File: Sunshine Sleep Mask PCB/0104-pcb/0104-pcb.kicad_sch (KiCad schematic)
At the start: 7 parts, among them J1 Conn_01x04, J2 Conn_01x02, J3 Conn_01x02, J4 Conn_02x15_Counter_Clockwise, U5 MAX98357A

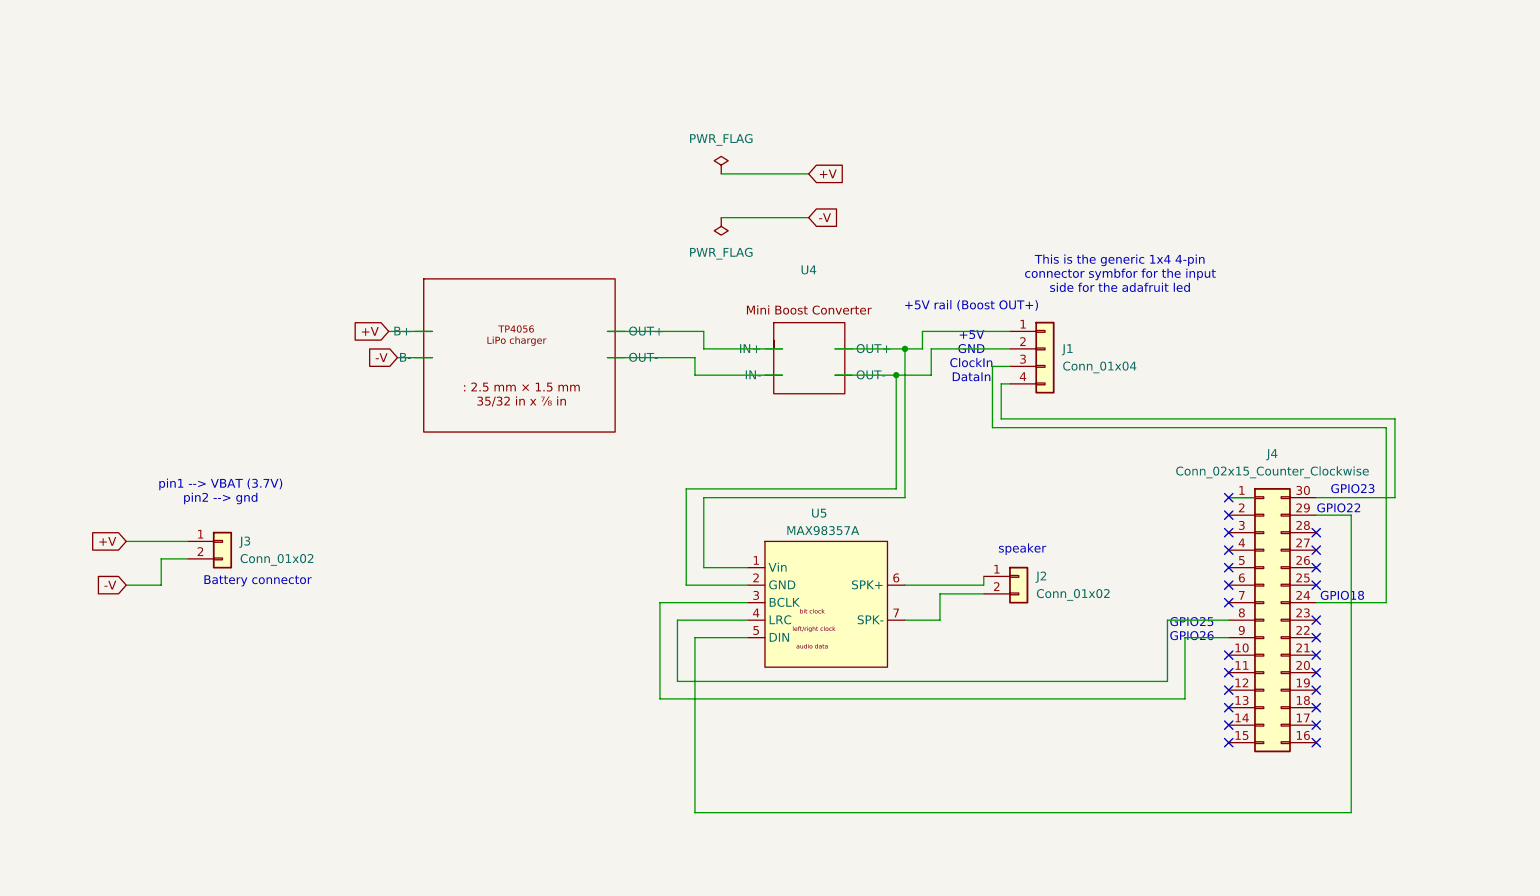
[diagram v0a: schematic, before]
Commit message: 0104- pcb + customized footprint
I created a new pcb editor + schematic where I copied the clay-0331. Then I made 3 customized footprints for the amplifier, charger LiPo, and for the boost converter. Similarly I was able to wire them in the pcb editor, yet there seems to be errors with the pcb constrains
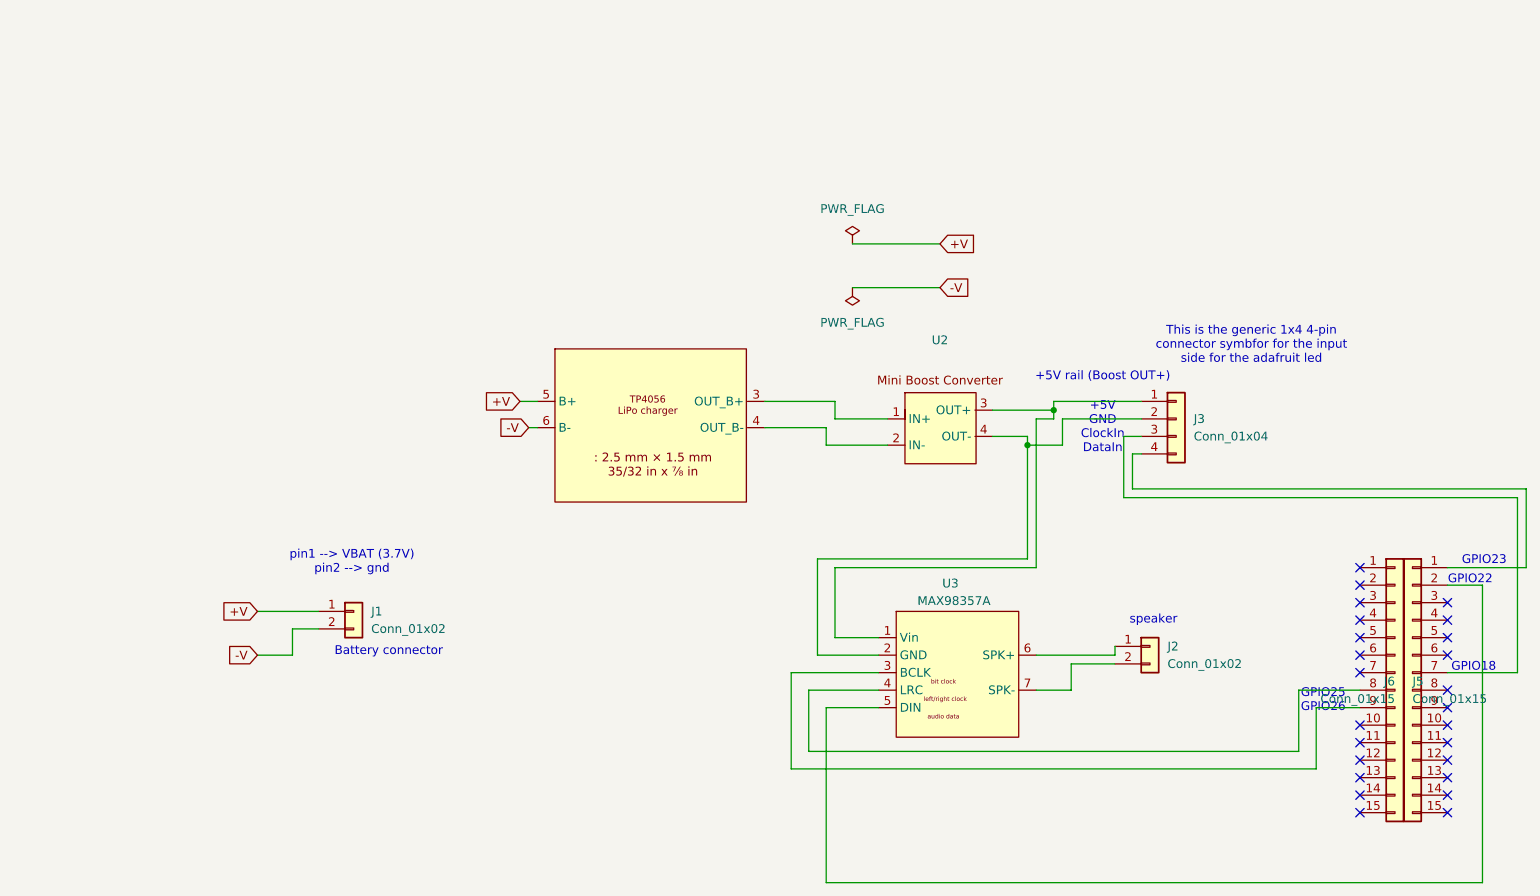
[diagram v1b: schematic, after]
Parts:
- removed J4: Conn_02x15_Counter_Clockwise, symbol Connector_Generic:Conn_02x15_Counter_Clockwise
- added J5, J6: Conn_01x15, Connector_PinSocket_2.54mm:PinSocket_1x15_P2.54mm_Vertical, symbol Connector_Generic:Conn_01x15
- U1: renamed from U3; footprint Connector_PinHeader_2.54mm:PinHeader_1x04_P2.54mm_Vertical -> Library_customized_0104:TP4056-18650
- U2: renamed from U4; footprint Connector_PinHeader_2.54mm:PinHeader_1x04_P2.54mm_Vertical -> Library_customized_0104:boost_converter
- U3: renamed from U5; footprint (none) -> Library_customized_0104:amplifier_github
- renumbered J3 to J1, J1 to J3
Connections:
- net +V: now also U1.5 (B+); no longer U1. (OUT-)
- net -V: now also U1.6 (B-); no longer U1. (OUT-)
- net at J3.1 (Pin_1), U3.1 (Vin): now also U2.3 (OUT+); no longer U2. (OUT-)
- net at J3.2 (Pin_2), U3.2 (GND): now also U2.4 (OUT-); no longer U2. (OUT-)
- net at U3.3 (BCLK): now also J5.9 (Pin_9)
- net at U3.4 (LRC): now also J5.8 (Pin_8)
- net at U3.5 (DIN): now also J6.2 (Pin_2)
- net at J3.3 (Pin_3): now also J6.7 (Pin_7)
- net at J3.4 (Pin_4): now also J6.1 (Pin_1)
- new net: U1.3 (OUT_B+), U2.1 (IN+)
- new net: U1.4 (OUT_B-), U2.2 (IN-)
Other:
- moved on the sheet: J1, J2, J3, U3

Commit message: Clay 0408 Changes
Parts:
- removed J2: Conn_01x02, Connector_PinHeader_2.54mm:PinHeader_1x02_P2.54mm_Vertical, symbol Connector_Generic:Conn_01x02
- removed J6: Conn_01x15, Connector_PinSocket_2.54mm:PinSocket_1x15_P2.54mm_Vertical, symbol Connector_Generic:Conn_01x15
- J5: value Conn_01x15 -> ESP32_WROOM; footprint Connector_PinSocket_2.54mm:PinSocket_1x15_P2.54mm_Vertical -> RF_Module:ESP32_WROOM_DevKit_30Pin_Custom
- U2: footprint Library_customized_0104:boost_converter -> Library_customized_0104:Boost_Converter_Clay_Custom
- U3: footprint Library_customized_0104:amplifier_github -> Library_customized_0104:adafruit-MAX98357
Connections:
- net at J3.1 (Pin_1), U2.3 (VOUT), U3.1 (Vin): now also J5.15 (VIN)
- net GND: now reaches J3.2 (Pin_2), U3.2 (GND)
- net GND: now also J5.14 (GND), J5.29 (GND), U1.4 (OUT-), U2.2 (GND); no longer U2.4 (OUT-)
- net at U3.3 (SV): no longer J5.9 (Pin_9)
- net at U3.4 (GAIN): no longer J5.8 (Pin_8)
- net at U3.5 (DIN): now also J5.26 (GPIO4)
- net at U3.6 (BCLK): now also J5.27 (GPIO2)
- net at U3.7 (LRC): now also J5.28 (GPIO15)
- net at J3.3 (Pin_3): now also J5.11 (GPIO14)
- net at J3.4 (Pin_4): now also J5.13 (GPIO13)
- no-connect marks 25 -> 28
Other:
- note removed: "+5V rail (Boost OUT+)"
- note removed: "GPIO18"
- note removed: "GPIO22"
- note removed: "GPIO23"
- note removed: "GPIO25"
- note removed: "GPIO26"
- note removed: "This is the generic 1x4 4-pin connector symbfor for the input side for the adafruit led"
- note removed: "speaker"
- moved on the sheet: J1, J3

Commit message: 7:30 04/08
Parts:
- U2: value ~ -> Boost Converter
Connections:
- net at U3.5 (DIN): now also J5.28 (GPIO15); no longer J5.26 (GPIO4)
- net at U3.7 (LRC): now also J5.26 (GPIO4); no longer J5.28 (GPIO15)
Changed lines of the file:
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@@
+	(wire
+		(pts
+			(xy 88.9 97.79) (xy 88.9 102.87)
+		)
+		(stroke
+			(width 0)
+			(type default)
+		)
+	)
 	(wire
 		(pts
@@
 	(wire
 		(pts
+			(xy 115.57 105.41) (xy 93.98 105.41)
+		)
+		(stroke
+			(width 0)
+			(type default)
+		)
+	)
+	(wire
+		(pts
 			(xy 41.91 107.95) (xy 41.91 104.14)
 		)
@@
 	(wire
 		(pts
-			(xy 113.03 102.87) (xy 93.98 102.87)
-		)
-		(stroke
-			(width 0)
-			(type default)
-		)
-	)
-	(wire
-		(pts
 			(xy 115.57 60.96) (xy 115.57 68.58)
 		)
@@
 	(wire
 		(pts
-			(xy 115.57 105.41) (xy 88.9 105.41)
-		)
-		(stroke
-			(width 0)
-			(type default)
-		)
-	)
-	(wire
-		(pts
 			(xy 115.57 68.58) (xy 143.51 68.58)
 		)
@@
 	(wire
 		(pts
-			(xy 93.98 97.79) (xy 93.98 102.87)
-		)
-		(stroke
-			(width 0)
-			(type default)
-		)
-	)
-	(wire
-		(pts
 			(xy 99.06 68.58) (xy 102.87 68.58)
 		)
@@
 	(wire
 		(pts
-			(xy 88.9 97.79) (xy 88.9 105.41)
-		)
-		(stroke
-			(width 0)
-			(type default)
-		)
-	)
-	(wire
-		(pts
 			(xy 143.51 95.25) (xy 118.11 95.25)
 		)
@@
 	(wire
 		(pts
+			(xy 93.98 97.79) (xy 93.98 105.41)
+		)
+		(stroke
+			(width 0)
+			(type default)
+		)
+	)
+	(wire
+		(pts
 			(xy 134.62 26.67) (xy 73.66 26.67)
+		)
+		(stroke
+			(width 0)
+			(type default)
+		)
+	)
+	(wire
+		(pts
+			(xy 88.9 102.87) (xy 113.03 102.87)
 		)
 		(stroke
@@
 		(on_board yes)
 		(dnp no)
-		(fields_autoplaced yes)
 		(property "Reference" "U2"
 			(at 123.19 40.64 0)
@@
 			)
 		)
-		(property "Value" "~"
+		(property "Value" "Boost Converter"
 			(at 123.19 43.18 0)
 			(effects
